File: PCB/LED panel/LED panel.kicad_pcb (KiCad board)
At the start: 2 copper layers, 20 parts

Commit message: LED panel PCB!
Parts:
- removed D11, D12, D13, D14, D15, D16, D17, D18, D19, D20: WS2812B, LED_SMD:LED_WS2812B_PLCC4_5.0x5.0mm_P3.2mm
- added ?: , , F.Cu at (50.1, 80.5)
- added REF**: TestPoint_THTPad_2.5x2.5mm_Drill1.2mm, TestPoint:TestPoint_THTPad_2.5x2.5mm_Drill1.2mm, F.Cu at (52.4, 114.3)
- added REF**: TestPoint_THTPad_2.5x2.5mm_Drill1.2mm, TestPoint:TestPoint_THTPad_2.5x2.5mm_Drill1.2mm, F.Cu at (47.6, 114.3)
- added REF**: TestPoint_THTPad_2.5x2.5mm_Drill1.2mm, TestPoint:TestPoint_THTPad_2.5x2.5mm_Drill1.2mm, F.Cu at (42.9, 114.3)
- moved D10 59.5 mm to (47.6, 32.1), turned to 180 degrees
- moved D9 58.1 mm to (47.6, 40.5), turned to 180 degrees
- moved D5 44.0 mm to (47.6, 73.8), turned to 180 degrees
- moved D6 37.6 mm to (47.6, 65.5), turned to 180 degrees
- moved D2 35.7 mm to (47.6, 98.8), turned to 180 degrees
- moved D1 35.7 mm to (47.6, 107.2), turned to 180 degrees
- moved D3 35.7 mm to (47.6, 90.5), turned to 180 degrees
- moved D4 35.7 mm to (47.6, 82.2), turned to 180 degrees
- moved D7 33.4 mm to (47.6, 57.1), turned to 180 degrees
- moved D8 32.3 mm to (47.6, 48.8), turned to 180 degrees
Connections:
- D10 pad 2: Net-(D10-DOUT) -> unconnected-(D10-DOUT-Pad2)
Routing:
- net Net-(D1-VSS): track 0.00 -> 118.9 mm
- net Net-(D1-VDD): track 0.00 -> 118.1 mm
- net Net-(D3-DOUT): track 0.00 -> 7.06 mm
- net Net-(D6-DOUT): track 0.00 -> 7.06 mm
- net Net-(D5-DOUT): track 0.00 -> 7.06 mm
- net Net-(D2-DOUT): track 0.00 -> 7.06 mm
- net Net-(D8-DOUT): track 0.00 -> 7.06 mm
- net Net-(D7-DOUT): track 0.00 -> 7.06 mm
- net Net-(D10-DIN): track 0.00 -> 7.06 mm
- net Net-(D4-DOUT): track 0.00 -> 7.06 mm
- net Net-(D1-DOUT): track 0.00 -> 7.06 mm
- net DIN: track 0.00 -> 6.51 mm
- added copper zone on F.Cu, net Net-(D1-VDD)
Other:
- board outline added: 14.3 x 93.6 mm
- board text added: "A Hack Club Highway Project!"
- board text added: "DIN"
- board text added: "GitHub @HenryLi-0"
- board text added: "LED PANEL"
- board text added: "RAVEN"
- board text added: "VDD"
- board text added: "VSS"

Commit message: 07012025 - pcb updates and some cad work!
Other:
- board size 14.3 x 93.6 mm -> 14.9 x 99.9 mm
- board text added: "OMG, LEDS!!! THE LED SUBSYSTEM IS THE MOST IMPORTANT SUBSYSTEM!!! YIPPEE, LEDS! :D"

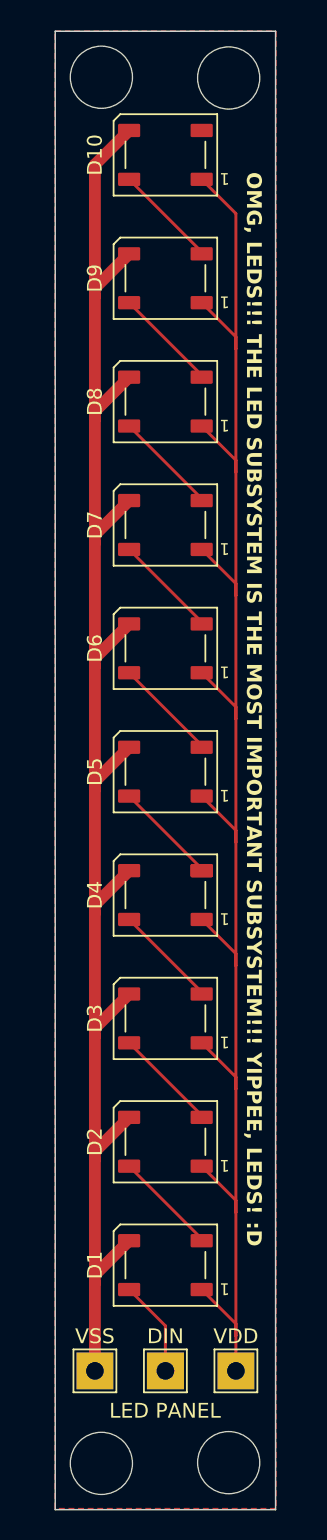
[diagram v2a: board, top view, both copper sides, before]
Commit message: update led panel and step files
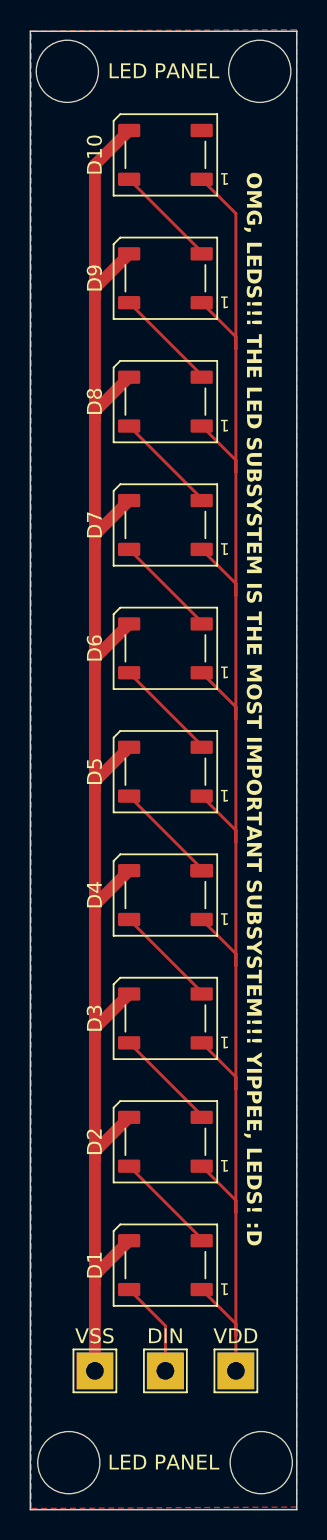
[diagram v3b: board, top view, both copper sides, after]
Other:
- board size 14.9 x 99.9 mm -> 18 x 99.9 mm

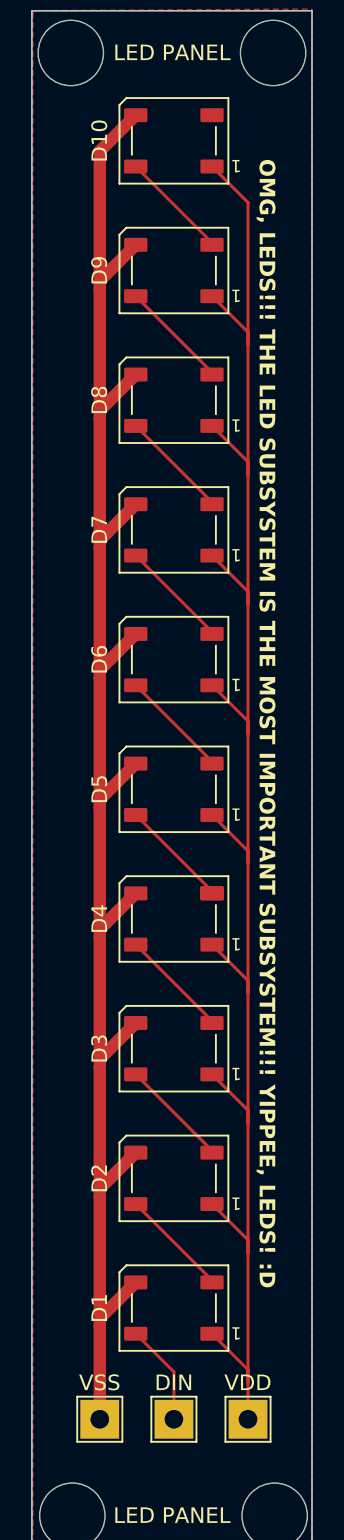
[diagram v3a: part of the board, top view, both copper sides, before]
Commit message: updated led panel
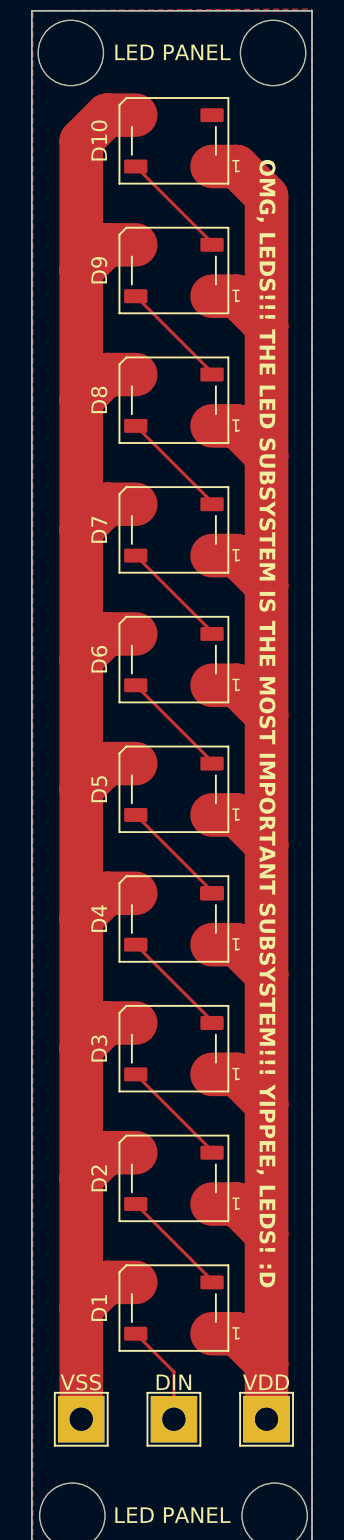
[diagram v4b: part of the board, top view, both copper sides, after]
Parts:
- removed the REF** at (52.4, 114.3)
- removed the REF** at (47.6, 114.3)
- removed the REF** at (42.9, 114.3)
- added REF**: TestPoint_THTPad_3.0x3.0mm_Drill1.5mm, TestPoint:TestPoint_THTPad_3.0x3.0mm_Drill1.5mm, F.Cu at (47.6, 114.3)
- added REF**: TestPoint_THTPad_3.0x3.0mm_Drill1.5mm, TestPoint:TestPoint_THTPad_3.0x3.0mm_Drill1.5mm, F.Cu at (53.6, 114.3)
- added REF**: TestPoint_THTPad_3.0x3.0mm_Drill1.5mm, TestPoint:TestPoint_THTPad_3.0x3.0mm_Drill1.5mm, F.Cu at (41.7, 114.3)
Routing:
- net Net-(D1-VSS): track 118.9 -> 124.0 mm
- net Net-(D1-VDD): track 118.1 -> 121.6 mm

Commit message: 07252025 - almost there!
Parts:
- removed ?: , 
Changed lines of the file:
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@@
 			)
 		)
+		(property ki_fp_filters "LED*WS2812*PLCC*5.0x5.0mm*P3.2mm*")
+		(sheetname "Root")
+		(sheetfile "LED panel.kicad_sch")
 		(attr smd)
 		(fp_line
@@
 			)
 		)
+		(property ki_fp_filters "LED*WS2812*PLCC*5.0x5.0mm*P3.2mm*")
+		(sheetname "Root")
+		(sheetfile "LED panel.kicad_sch")
 		(attr smd)
 		(fp_line
@@
 			)
 		)
+		(property ki_fp_filters "LED*WS2812*PLCC*5.0x5.0mm*P3.2mm*")
+		(sheetname "Root")
+		(sheetfile "LED panel.kicad_sch")
 		(attr smd)
 		(fp_line
@@
 			)
 		)
+		(property ki_fp_filters "LED*WS2812*PLCC*5.0x5.0mm*P3.2mm*")
+		(sheetname "Root")
+		(sheetfile "LED panel.kicad_sch")
 		(attr smd)
 		(fp_line
@@
 		)
 	)
-	(footprint ""
-		(layer "F.Cu")
-		(at 50.075 80.503125)
-		(property "Reference" ""
-			(at 0 0 0)
-			(layer "F.SilkS")
-			(effects
-				(font
-					(size 1.27 1.27)
-					(thickness 0.15)
-				)
-			)
-		)
-		(property "Value" ""
-			(at 0 0 0)
-			(layer "F.Fab")
-			(effects
-				(font
-					(size 1.27 1.27)
-					(thickness 0.15)
-				)
-			)
-		)
-		(property "Footprint" ""
-			(at 0 0 0)
-			(layer "F.Fab")
-			(hide yes)
-			(effects
-				(font
-					(size 1.27 1.27)
-					(thickness 0.15)
-				)
-			)
-		)
-		(property "Datasheet" ""
-			(at 0 0 0)
-			(layer "F.Fab")
-			(hide yes)
-			(effects
-				(font
-					(size 1.27 1.27)
-					(thickness 0.15)
-				)
-			)
-		)
-		(property "Description" ""
-			(at 0 0 0)
-			(layer "F.Fab")
-			(hide yes)
-			(effects
-				(font
-					(size 1.27 1.27)
-					(thickness 0.15)
-				)
-			)
-		)
-		(pad "2" smd roundrect
-			(at 0 0 180)
-			(size 1.5 0.9)
-			(layers "F.Cu" "F.Paste" "F.Mask")
-			(roundrect_rratio 0.1)
-			(net 7 "Net-(D4-DOUT)")
-			(pinfunction "DOUT")
-			(pintype "output")
-		)
-	)
 	(footprint "LED_SMD:LED_WS2812B_PLCC4_5.0x5.0mm_P3.2mm"
 		(layer "F.Cu")
@@
 			)
 		)
+		(property ki_fp_filters "LED*WS2812*PLCC*5.0x5.0mm*P3.2mm*")
+		(sheetname "Root")
+		(sheetfile "LED panel.kicad_sch")
 		(attr smd)
 		(fp_line
@@
 			)
 		)
+		(property ki_fp_filters "LED*WS2812*PLCC*5.0x5.0mm*P3.2mm*")
+		(sheetname "Root")
+		(sheetfile "LED panel.kicad_sch")
 		(attr smd)
 		(fp_line
@@
 			)
 		)
+		(property ki_fp_filters "LED*WS2812*PLCC*5.0x5.0mm*P3.2mm*")
+		(sheetname "Root")
+		(sheetfile "LED panel.kicad_sch")
 		(attr smd)
 		(fp_line
@@
 	(footprint "LED_SMD:LED_WS2812B_PLCC4_5.0x5.0mm_P3.2mm"
 		(layer "F.Cu")
-		(at 47.625 82.153125 180)
+		(at 47.62504 82.153194 180)
 		(descr "5.0mm x 5.0mm Addressable RGB LED NeoPixel, https://cdn-shop.adafruit.com/datasheets/WS2812B.pdf")
 		(tags "LED RGB NeoPixel PLCC-4 5050")
@@
 			)
 		)
+		(property ki_fp_filters "LED*WS2812*PLCC*5.0x5.0mm*P3.2mm*")
+		(sheetname "Root")
+		(sheetfile "LED panel.kicad_sch")
 		(attr smd)
 		(fp_line
@@
 			)
 		)
+		(property ki_fp_filters "LED*WS2812*PLCC*5.0x5.0mm*P3.2mm*")
+		(sheetname "Root")
+		(sheetfile "LED panel.kicad_sch")
 		(attr smd)
 		(fp_line
@@
 			)
 		)
+		(property ki_fp_filters "LED*WS2812*PLCC*5.0x5.0mm*P3.2mm*")
+		(sheetname "Root")
+		(sheetfile "LED panel.kicad_sch")
 		(attr smd)
 		(fp_line
@@
 	)
 	(segment
-		(start 50.075 80.36875)
-		(end 50.075 80.503125)
+		(start 45.175 75.46875)
+		(end 50.075 80.36875)
 		(width 0.2)
 		(layer "F.Cu")
@@
 	)
 	(segment
-		(start 45.175 75.46875)
-		(end 50.075 80.36875)
+		(start 50.075 80.36875)
+		(end 50.075 80.503125)
 		(width 0.2)
 		(layer "F.Cu")
